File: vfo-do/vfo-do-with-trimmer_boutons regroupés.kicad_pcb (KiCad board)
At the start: 2 copper layers, 19 parts, among them J1 Fréquence, J10 GPS, J2 Bande, J3 Reset, J4 Résolution, J5 Si5351, J8 LCD, J9 Alim +12V, U1 L7805

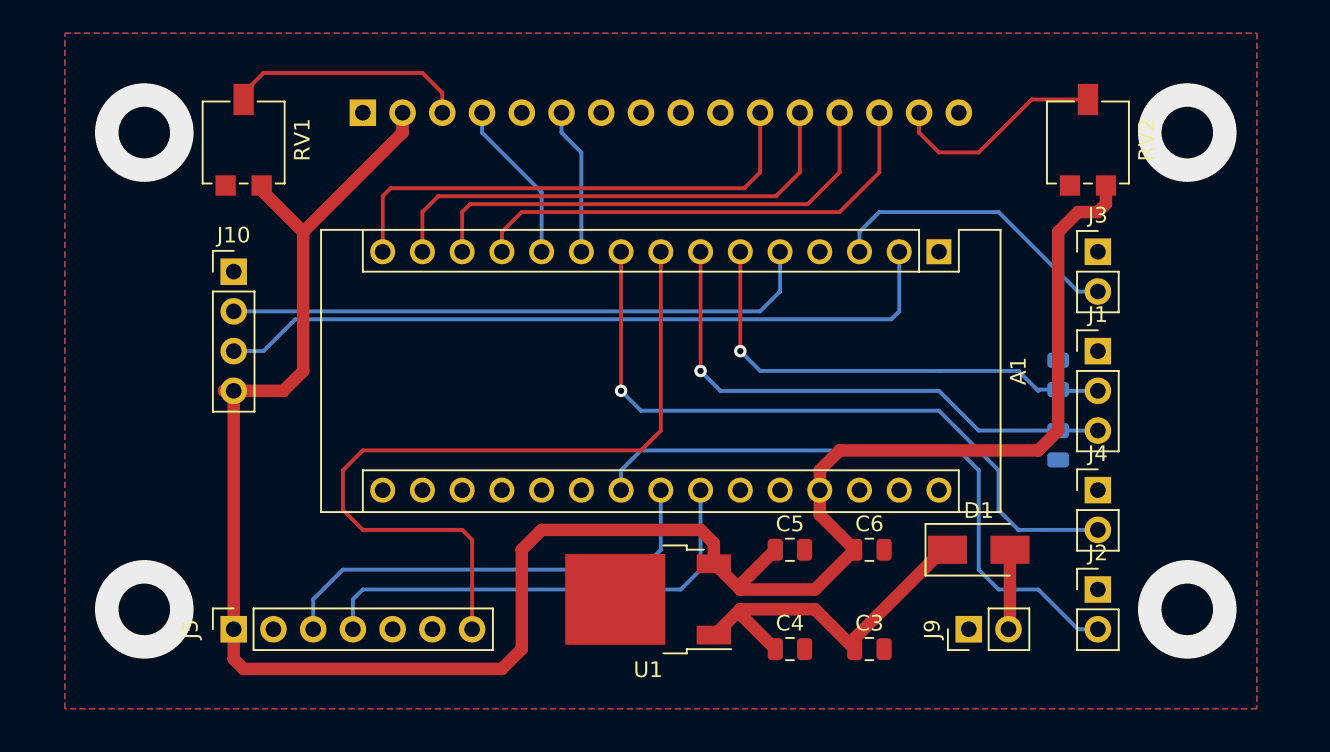
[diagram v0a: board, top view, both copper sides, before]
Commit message: Amélioration du routage, perçage de fixation
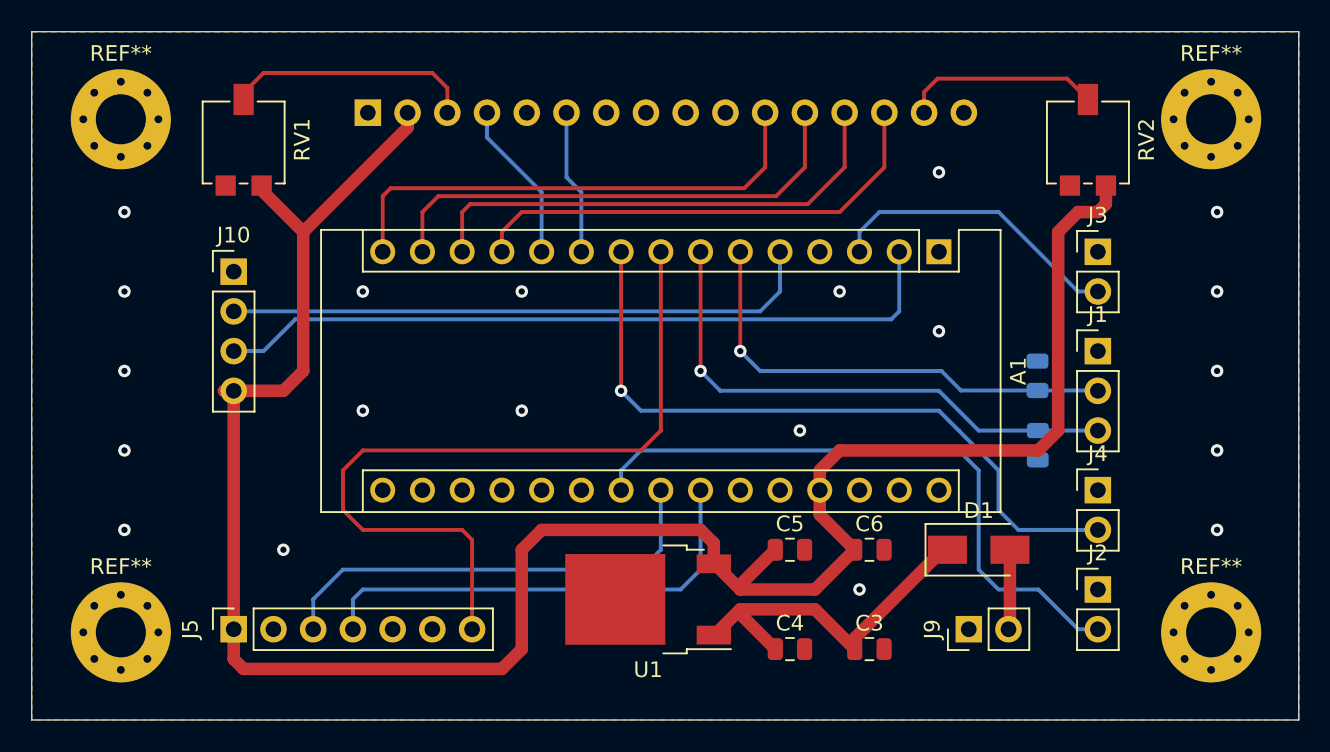
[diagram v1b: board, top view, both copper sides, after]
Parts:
- added REF**: MountingHole_3.2mm_M3_Pad_Via, MountingHole:MountingHole_3.2mm_M3_Pad_Via, F.Cu at (74.7, 43.6)
- added REF**: MountingHole_3.2mm_M3_Pad_Via, MountingHole:MountingHole_3.2mm_M3_Pad_Via, F.Cu at (74.7, 76.4)
- added REF**: MountingHole_3.2mm_M3_Pad_Via, MountingHole:MountingHole_3.2mm_M3_Pad_Via, F.Cu at (144.4, 76.4)
- added REF**: MountingHole_3.2mm_M3_Pad_Via, MountingHole:MountingHole_3.2mm_M3_Pad_Via, F.Cu at (144.4, 43.6)
- moved C2 1.32 mm to (133.3, 60.0)
- moved C1 1.30 mm to (133.3, 64.4)
- moved J8 0.32 mm to (90.5, 43.2)
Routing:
- net A: track 14.0 -> 12.7 mm
- net V0: track 15.4 -> 16.0 mm
- net GND: vias 4 -> 20
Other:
- board outline added: 81 x 44 mm
